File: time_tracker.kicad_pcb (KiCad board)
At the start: 2 copper layers, 149 x 43 mm, 15 parts, among them U1 max7219cng, U2 max7219cng, U3 XIAO ESP32C3

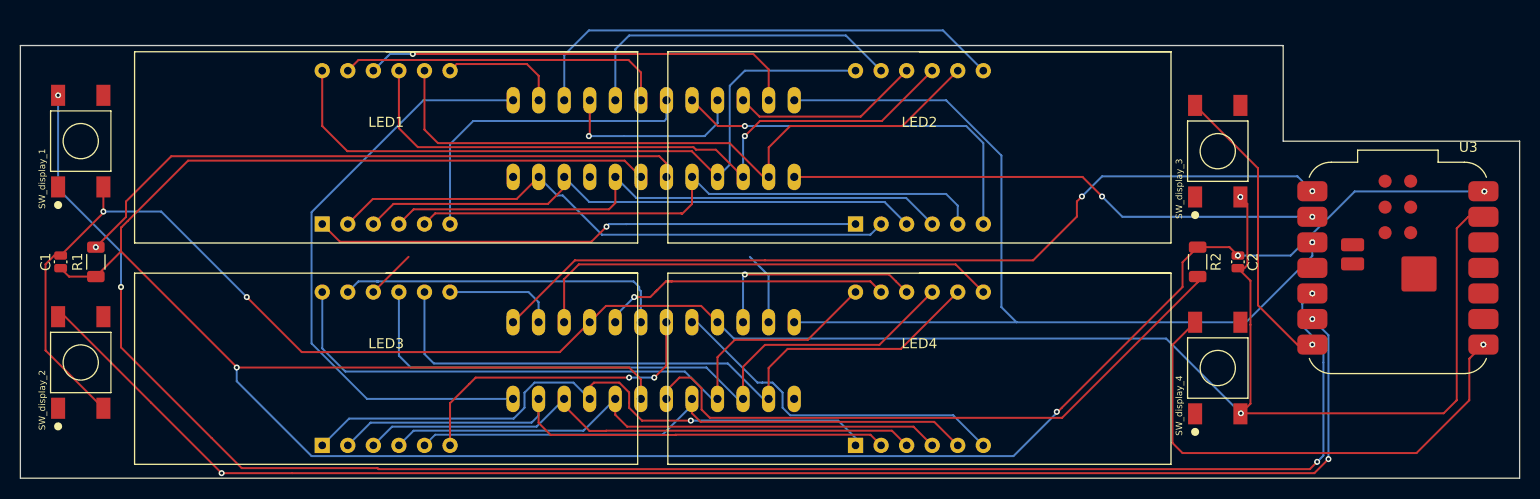
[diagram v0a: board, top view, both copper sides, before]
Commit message: added rtc, battery circuit
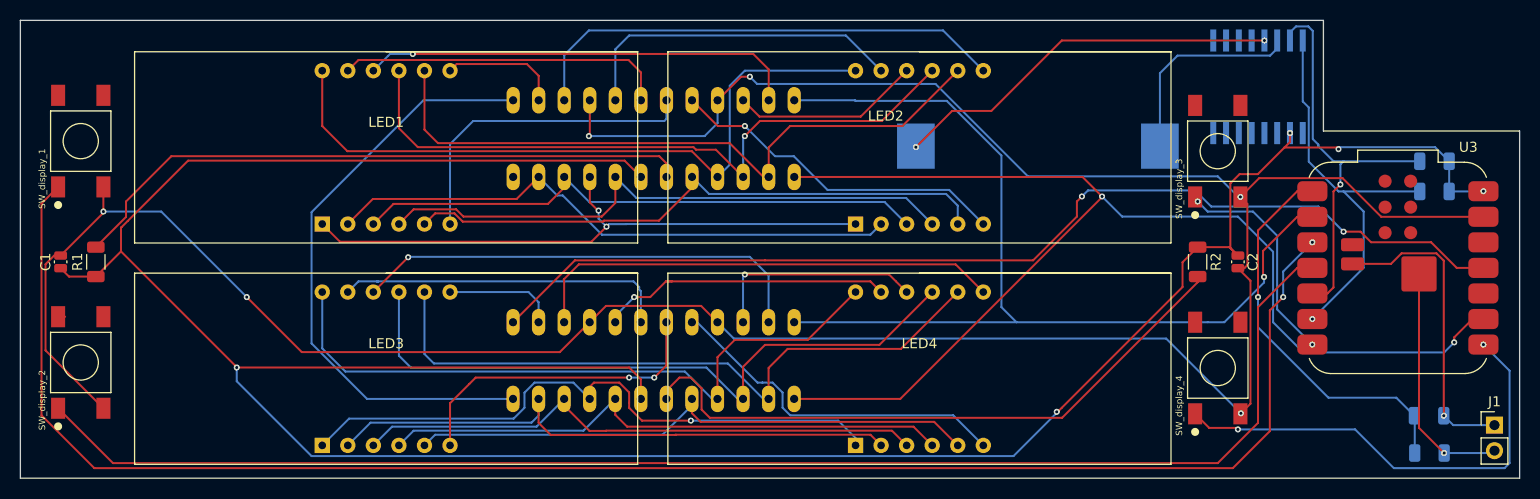
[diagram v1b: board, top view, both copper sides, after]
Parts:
- added BT1: BAT-HLD-010-SMT-TR, cr2032 holder:BAT_BAT-HLD-010-SMT-TR, B.Cu at (126.1, 89.5)
- added IC1: DS3231, DS3231:SO16W, B.Cu at (148.0, 83.6)
- added J1: Conn_01x02_Pin, Connector_PinHeader_2.54mm:PinHeader_1x02_P2.54mm_Vertical, F.Cu at (171.5, 117.2)
- added R3: 220k, Resistor_SMD:R_1206_3216Metric, B.Cu at (165.0, 120.0)
- added R4: 220k, Resistor_SMD:R_1206_3216Metric, B.Cu at (165.0, 116.3)
- added R5: 10k, Resistor_SMD:R_1206_3216Metric, B.Cu at (165.5, 94.0)
- added R6: 10k, Resistor_SMD:R_1206_3216Metric, B.Cu at (165.5, 91.0)
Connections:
- SW_display_1 pad 1: unconnected-(SW_display_1-Pad1) -> /SW_1
- SW_display_1 pad 2: /SW_1 -> unconnected-(SW_display_1-Pad2)
- SW_display_2 pad 1: unconnected-(SW_display_2-Pad1) -> /SW_2
- SW_display_2 pad 2: /SW_2 -> unconnected-(SW_display_2-Pad2)
- SW_display_3 pad 1: unconnected-(SW_display_3-Pad1) -> /SW_3
- SW_display_3 pad 2: /SW_3 -> unconnected-(SW_display_3-Pad2)
- SW_display_4 pad 1: unconnected-(SW_display_4-Pad1) -> /SW_4
- SW_display_4 pad 2: /SW_4 -> unconnected-(SW_display_4-Pad2)
- U3 pad 1: /driver_input -> /Battery_voltage
- U3 pad 11: unconnected-(U3-D10-Pad11) -> /driver_input
- U3 pad 15: unconnected-(U3-BAT+-Pad15) -> /Battery_+
- U3 pad 16: unconnected-(U3-BAT--Pad16) -> /Battery_-
- U3 pad 2: /driver_clock -> /driver_load
- U3 pad 3: /driver_load -> /SW_1
- U3 pad 4: unconnected-(U3-D3-Pad4) -> /SW_2
- U3 pad 5: /SW_1 -> /SDA
- U3 pad 6: /SW_2 -> /SDL
- U3 pad 9: unconnected-(U3-D8-Pad9) -> /driver_clock
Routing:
- net /driver_clock: track 53.1 -> 120.5 mm
- net GND: track 237.3 -> 279.5 mm, vias 5 -> 6
- net /SDA: track 0.00 -> 41.2 mm, vias 0 -> 1
- net /SDL: track 0.00 -> 40.2 mm, vias 0 -> 1
- net /Battery_voltage: track 0.00 -> 39.5 mm, vias 0 -> 1
- net Net-(IC1-GND): track 0.00 -> 39.0 mm, vias 0 -> 2
- net /driver_1_digit_1: track 12.2 -> 46.2 mm, vias 0 -> 1
- net /Battery_-: track 0.00 -> 30.6 mm, vias 0 -> 1
- net /Battery_+: track 0.00 -> 23.9 mm, vias 0 -> 1
- net Net-(IC1-VBAT): track 0.00 -> 19.7 mm
- net /driver_input: track 86.9 -> 105.9 mm
- net VCC: track 265.3 -> 277.7 mm, vias 4 -> 5
- net /SW_3: track 29.5 -> 22.1 mm, vias 1 -> 2
- net /SW_2: track 147.9 -> 141.7 mm, vias 3 -> 0
- net /driver_0_seg_e: track 54.5 -> 60.2 mm, vias 1 -> 2
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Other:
- board size 149 x 43 mm -> 149 x 45.5 mm
